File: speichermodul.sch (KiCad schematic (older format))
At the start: 65 parts, among them IC1 6116, P1 CONN_3X2, P2 CONN_01X01, P3 CONN_01X01, P4 CONN_01X01, P5 CONN_01X01, P6 CONN_01X01, P7 CONN_01X01, P8 CONN_02X10, P9 CONN_02X10, SW1 SW_PUSH, SW2 SW_PUSH, U1 7400, U2 74LS08, U3 74LS08, U4 74LS14, U5 74LS540, U6 74LS540

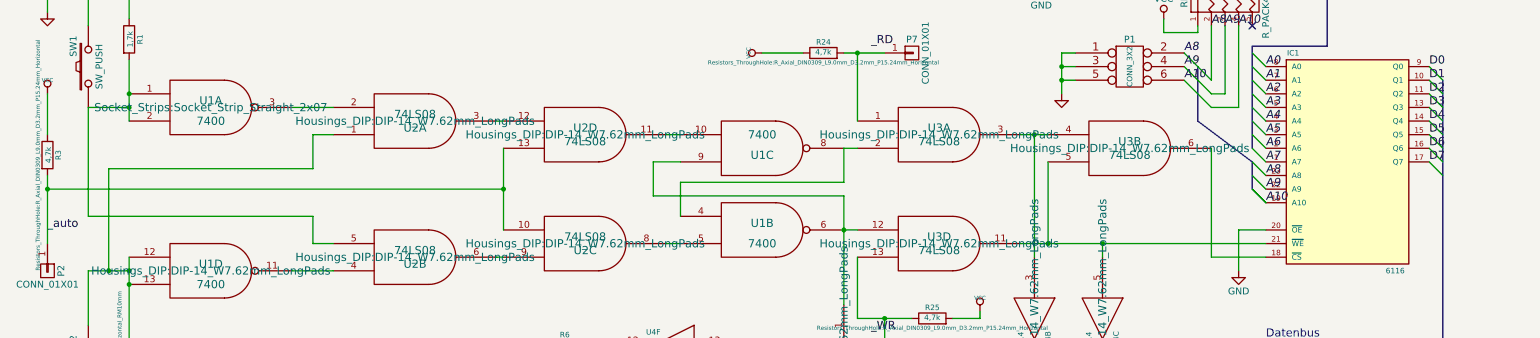
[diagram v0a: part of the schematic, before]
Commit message: Bauteile hinzugefügt
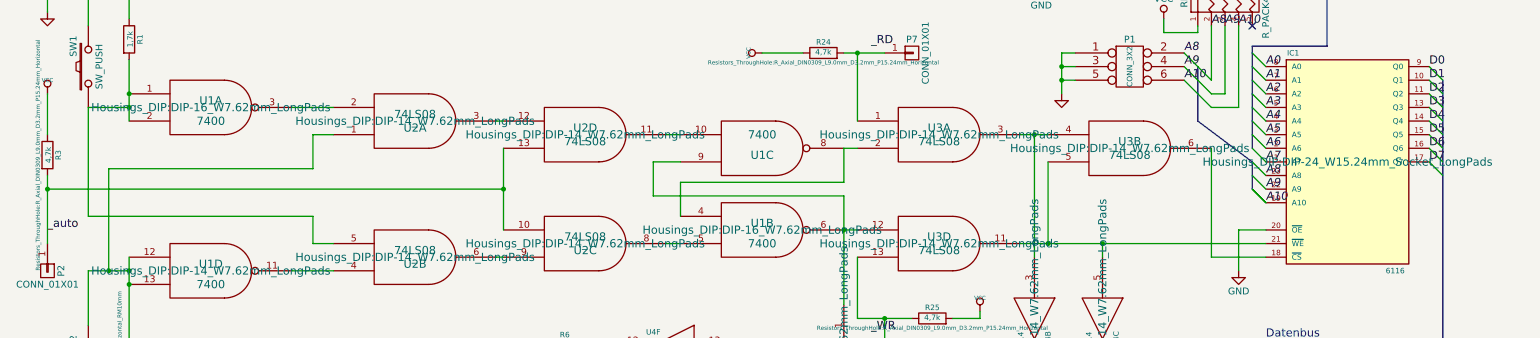
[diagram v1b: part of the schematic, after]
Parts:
- IC1: footprint (none) -> Housings_DIP:DIP-24_W15.24mm_Socket_LongPads
- U1: footprint Socket_Strips:Socket_Strip_Straight_2x07 -> Housings_DIP:DIP-16_W7.62mm_LongPads
- U1: footprint (none) -> Housings_DIP:DIP-16_W7.62mm_LongPads
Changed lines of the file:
@@
 F 0 "U1" H 1900 3000 60  0000 C CNN
 F 1 "7400" H 1900 2850 60  0000 C CNN
-F 2 "Socket_Strips:Socket_Strip_Straight_2x07" H 1900 2950 60  0000 C CNN
+F 2 "Housings_DIP:DIP-16_W7.62mm_LongPads" H 1900 2950 60  0000 C CNN
 F 3 "~" H 1900 2950 60  0000 C CNN
 	1    1900 2950
@@
 F 0 "U1" H 5950 3900 60  0000 C CNN
 F 1 "7400" H 5950 3750 60  0000 C CNN
-F 2 "" H 5950 3850 60  0001 C CNN
+F 2 "Housings_DIP:DIP-16_W7.62mm_LongPads" H 5950 3850 60  0000 C CNN
 F 3 "~" H 5950 3850 60  0000 C CNN
 	2    5950 3850
@@
 F 0 "U1" H 5950 3300 60  0000 C CNN
 F 1 "7400" H 5950 3150 60  0000 C CNN
-F 2 "" H 5950 3250 60  0001 C CNN
+F 2 "Housings_DIP:DIP-16_W7.62mm_LongPads" H 5950 3250 60  0001 C CNN
 F 3 "~" H 5950 3250 60  0000 C CNN
 	3    5950 3250
@@
 F 0 "IC1" H 9850 4150 40  0000 C CNN
 F 1 "6116" H 10600 2550 40  0000 C CNN
-F 2 "" H 10250 3350 60  0001 C CNN
+F 2 "Housings_DIP:DIP-24_W15.24mm_Socket_LongPads" H 10250 3350 60  0000 C CNN
 F 3 "" H 10250 3350 60  0000 C CNN
 	1    10250 3350

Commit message: einige Leds und Resistoren hinzugefügt und ausgebessert
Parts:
- D10, D11, D12, D13, D14, D15, D16, D17, D18, D4, D5, D6, D7, D8, D9: footprint (none) -> LEDs:LED_D1.8mm_W1.8mm_H2.4mm_Horizontal_O3.81mm_Z8.2mm
- D3: footprint LEDs:LED-3MM -> LEDs:LED_D1.8mm_W1.8mm_H2.4mm_Horizontal_O3.81mm_Z8.2mm
- R10, R11, R12, R13, R14, R15, R4, R9: footprint (none) -> Resistors_ThroughHole:R_Axial_DIN0411_L9.9mm_D3.6mm_P15.24mm_Horizontal
- U1: footprint Housings_DIP:DIP-16_W7.62mm_LongPads -> Housings_DIP:DIP-14_W7.62mm_LongPads
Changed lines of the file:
@@
 F 0 "U1" H 1900 3000 60  0000 C CNN
 F 1 "7400" H 1900 2850 60  0000 C CNN
-F 2 "Housings_DIP:DIP-16_W7.62mm_LongPads" H 1900 2950 60  0000 C CNN
+F 2 "Housings_DIP:DIP-14_W7.62mm_LongPads" H 1900 2950 60  0000 C CNN
 F 3 "~" H 1900 2950 60  0000 C CNN
 	1    1900 2950
@@
 F 0 "U1" H 5950 3900 60  0000 C CNN
 F 1 "7400" H 5950 3750 60  0000 C CNN
-F 2 "Housings_DIP:DIP-16_W7.62mm_LongPads" H 5950 3850 60  0000 C CNN
+F 2 "Housings_DIP:DIP-14_W7.62mm_LongPads" H 5950 3850 60  0000 C CNN
 F 3 "~" H 5950 3850 60  0000 C CNN
 	2    5950 3850
@@
 F 0 "U1" H 5950 3300 60  0000 C CNN
 F 1 "7400" H 5950 3150 60  0000 C CNN
-F 2 "Housings_DIP:DIP-16_W7.62mm_LongPads" H 5950 3250 60  0001 C CNN
+F 2 "Housings_DIP:DIP-14_W7.62mm_LongPads" H 5950 3250 60  0000 C CNN
 F 3 "~" H 5950 3250 60  0000 C CNN
 	3    5950 3250
@@
 F 0 "R4" V 2830 5650 50  0000 C CNN
 F 1 "330" V 2750 5650 50  0000 C CNN
-F 2 "" V 2680 5650 30  0001 C CNN
+F 2 "Resistors_ThroughHole:R_Axial_DIN0411_L9.9mm_D3.6mm_P15.24mm_Horizontal" V 2680 5650 30  0000 C CNN
 F 3 "" H 2750 5650 30  0000 C CNN
 	1    2750 5650
@@
 F 0 "R9" V 2830 5750 50  0000 C CNN
 F 1 "330" V 2750 5750 50  0000 C CNN
-F 2 "" V 2680 5750 30  0001 C CNN
+F 2 "Resistors_ThroughHole:R_Axial_DIN0411_L9.9mm_D3.6mm_P15.24mm_Horizontal" V 2680 5750 30  0000 C CNN
 F 3 "" H 2750 5750 30  0000 C CNN
 	1    2750 5750
@@
 F 0 "R10" V 2830 5850 50  0000 C CNN
 F 1 "330" V 2750 5850 50  0000 C CNN
-F 2 "" V 2680 5850 30  0001 C CNN
+F 2 "Resistors_ThroughHole:R_Axial_DIN0411_L9.9mm_D3.6mm_P15.24mm_Horizontal" V 2680 5850 30  0000 C CNN
 F 3 "" H 2750 5850 30  0000 C CNN
 	1    2750 5850
@@
 F 0 "R11" V 2830 5950 50  0000 C CNN
 F 1 "330" V 2750 5950 50  0000 C CNN
-F 2 "" V 2680 5950 30  0001 C CNN
+F 2 "Resistors_ThroughHole:R_Axial_DIN0411_L9.9mm_D3.6mm_P15.24mm_Horizontal" V 2680 5950 30  0000 C CNN
 F 3 "" H 2750 5950 30  0000 C CNN
 	1    2750 5950
@@
 F 0 "R12" V 2830 6050 50  0000 C CNN
 F 1 "330" V 2750 6050 50  0000 C CNN
-F 2 "" V 2680 6050 30  0001 C CNN
+F 2 "Resistors_ThroughHole:R_Axial_DIN0411_L9.9mm_D3.6mm_P15.24mm_Horizontal" V 2680 6050 30  0000 C CNN
 F 3 "" H 2750 6050 30  0000 C CNN
 	1    2750 6050
@@
 F 0 "R13" V 2830 6150 50  0000 C CNN
 F 1 "330" V 2750 6150 50  0000 C CNN
-F 2 "" V 2680 6150 30  0001 C CNN
+F 2 "Resistors_ThroughHole:R_Axial_DIN0411_L9.9mm_D3.6mm_P15.24mm_Horizontal" V 2680 6150 30  0000 C CNN
 F 3 "" H 2750 6150 30  0000 C CNN
 	1    2750 6150
@@
 F 0 "R14" V 2830 6250 50  0000 C CNN
 F 1 "330" V 2750 6250 50  0000 C CNN
-F 2 "" V 2680 6250 30  0001 C CNN
+F 2 "Resistors_ThroughHole:R_Axial_DIN0411_L9.9mm_D3.6mm_P15.24mm_Horizontal" V 2680 6250 30  0000 C CNN
 F 3 "" H 2750 6250 30  0000 C CNN
 	1    2750 6250
@@
 F 0 "R15" V 2830 6350 50  0000 C CNN
 F 1 "330" V 2750 6350 50  0000 C CNN
-F 2 "" V 2680 6350 30  0001 C CNN
+F 2 "Resistors_ThroughHole:R_Axial_DIN0411_L9.9mm_D3.6mm_P15.24mm_Horizontal" V 2680 6350 30  0000 C CNN
 F 3 "" H 2750 6350 30  0000 C CNN
 	1    2750 6350
@@
 F 0 "D3" H 2350 5750 50  0000 C CNN
 F 1 "LED" H 2350 5550 50  0000 C CNN
-F 2 "LEDs:LED-3MM" H 2350 5650 60  0000 C CNN
+F 2 "LEDs:LED_D1.8mm_W1.8mm_H2.4mm_Horizontal_O3.81mm_Z8.2mm" H 2350 5650 60  0000 C CNN
 F 3 "" H 2350 5650 60  0000 C CNN
 	1    2350 5650
@@
 F 0 "D4" H 2350 5850 50  0000 C CNN
 F 1 "LED" H 2350 5650 50  0000 C CNN
-F 2 "" H 2350 5750 60  0001 C CNN
+F 2 "LEDs:LED_D1.8mm_W1.8mm_H2.4mm_Horizontal_O3.81mm_Z8.2mm" H 2350 5750 60  0000 C CNN
 F 3 "" H 2350 5750 60  0000 C CNN
 	1    2350 5750
@@
 F 0 "D5" H 2350 5950 50  0000 C CNN
 F 1 "LED" H 2350 5750 50  0000 C CNN
-F 2 "" H 2350 5850 60  0001 C CNN
+F 2 "LEDs:LED_D1.8mm_W1.8mm_H2.4mm_Horizontal_O3.81mm_Z8.2mm" H 2350 5850 60  0000 C CNN
 F 3 "" H 2350 5850 60  0000 C CNN
 	1    2350 5850
@@
 F 0 "D6" H 2350 6050 50  0000 C CNN
 F 1 "LED" H 2350 5850 50  0000 C CNN
-F 2 "" H 2350 5950 60  0001 C CNN
+F 2 "LEDs:LED_D1.8mm_W1.8mm_H2.4mm_Horizontal_O3.81mm_Z8.2mm" H 2350 5950 60  0000 C CNN
 F 3 "" H 2350 5950 60  0000 C CNN
 	1    2350 5950
@@
 F 0 "D7" H 2350 6150 50  0000 C CNN
 F 1 "LED" H 2350 5950 50  0000 C CNN
-F 2 "" H 2350 6050 60  0001 C CNN
+F 2 "LEDs:LED_D1.8mm_W1.8mm_H2.4mm_Horizontal_O3.81mm_Z8.2mm" H 2350 6050 60  0000 C CNN
 F 3 "" H 2350 6050 60  0000 C CNN
 	1    2350 6050
@@
 F 0 "D8" H 2350 6250 50  0000 C CNN
 F 1 "LED" H 2350 6050 50  0000 C CNN
-F 2 "" H 2350 6150 60  0001 C CNN
+F 2 "LEDs:LED_D1.8mm_W1.8mm_H2.4mm_Horizontal_O3.81mm_Z8.2mm" H 2350 6150 60  0000 C CNN
 F 3 "" H 2350 6150 60  0000 C CNN
 	1    2350 6150
@@
 F 0 "D9" H 2350 6350 50  0000 C CNN
 F 1 "LED" H 2350 6150 50  0000 C CNN
-F 2 "" H 2350 6250 60  0001 C CNN
+F 2 "LEDs:LED_D1.8mm_W1.8mm_H2.4mm_Horizontal_O3.81mm_Z8.2mm" H 2350 6250 60  0000 C CNN
 F 3 "" H 2350 6250 60  0000 C CNN
 	1    2350 6250
@@
 F 0 "D10" H 2350 6450 50  0000 C CNN
 F 1 "LED" H 2350 6250 50  0000 C CNN
-F 2 "" H 2350 6350 60  0001 C CNN
+F 2 "LEDs:LED_D1.8mm_W1.8mm_H2.4mm_Horizontal_O3.81mm_Z8.2mm" H 2350 6350 60  0000 C CNN
 F 3 "" H 2350 6350 60  0000 C CNN
 	1    2350 6350
@@
 F 0 "D11" H 6000 1050 50  0000 C CNN
 F 1 "LED" H 6000 850 50  0000 C CNN
-F 2 "" H 6000 950 60  0001 C CNN
+F 2 "LEDs:LED_D1.8mm_W1.8mm_H2.4mm_Horizontal_O3.81mm_Z8.2mm" H 6000 950 60  0000 C CNN
 F 3 "" H 6000 950 60  0000 C CNN
 	1    6000 950
@@
 F 0 "D12" H 6000 1150 50  0000 C CNN
 F 1 "LED" H 6000 950 50  0000 C CNN
-F 2 "" H 6000 1050 60  0001 C CNN
+F 2 "LEDs:LED_D1.8mm_W1.8mm_H2.4mm_Horizontal_O3.81mm_Z8.2mm" H 6000 1050 60  0000 C CNN
 F 3 "" H 6000 1050 60  0000 C CNN
 	1    6000 1050
@@
 F 0 "D13" H 6000 1250 50  0000 C CNN
 F 1 "LED" H 6000 1050 50  0000 C CNN
-F 2 "" H 6000 1150 60  0001 C CNN
+F 2 "LEDs:LED_D1.8mm_W1.8mm_H2.4mm_Horizontal_O3.81mm_Z8.2mm" H 6000 1150 60  0000 C CNN
 F 3 "" H 6000 1150 60  0000 C CNN
 	1    6000 1150
@@
 F 0 "D14" H 6000 1350 50  0000 C CNN
 F 1 "LED" H 6000 1150 50  0000 C CNN
-F 2 "" H 6000 1250 60  0001 C CNN
+F 2 "LEDs:LED_D1.8mm_W1.8mm_H2.4mm_Horizontal_O3.81mm_Z8.2mm" H 6000 1250 60  0000 C CNN
 F 3 "" H 6000 1250 60  0000 C CNN
 	1    6000 1250
@@
 F 0 "D15" H 6000 1450 50  0000 C CNN
 F 1 "LED" H 6000 1250 50  0000 C CNN
-F 2 "" H 6000 1350 60  0001 C CNN
+F 2 "LEDs:LED_D1.8mm_W1.8mm_H2.4mm_Horizontal_O3.81mm_Z8.2mm" H 6000 1350 60  0000 C CNN
 F 3 "" H 6000 1350 60  0000 C CNN
 	1    6000 1350
@@
 F 0 "D16" H 6000 1550 50  0000 C CNN
 F 1 "LED" H 6000 1350 50  0000 C CNN
-F 2 "" H 6000 1450 60  0001 C CNN
+F 2 "LEDs:LED_D1.8mm_W1.8mm_H2.4mm_Horizontal_O3.81mm_Z8.2mm" H 6000 1450 60  0000 C CNN
 F 3 "" H 6000 1450 60  0000 C CNN
 	1    6000 1450
@@
 F 0 "D17" H 6000 1650 50  0000 C CNN
 F 1 "LED" H 6000 1450 50  0000 C CNN
-F 2 "" H 6000 1550 60  0001 C CNN
+F 2 "LEDs:LED_D1.8mm_W1.8mm_H2.4mm_Horizontal_O3.81mm_Z8.2mm" H 6000 1550 60  0000 C CNN
 F 3 "" H 6000 1550 60  0000 C CNN
 	1    6000 1550
@@
 F 0 "D18" H 6000 1750 50  0000 C CNN
 F 1 "LED" H 6000 1550 50  0000 C CNN
-F 2 "" H 6000 1650 60  0001 C CNN
+F 2 "LEDs:LED_D1.8mm_W1.8mm_H2.4mm_Horizontal_O3.81mm_Z8.2mm" H 6000 1650 60  0000 C CNN
 F 3 "" H 6000 1650 60  0000 C CNN
 	1    6000 1650
